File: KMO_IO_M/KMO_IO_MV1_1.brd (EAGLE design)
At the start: 84.5 x 96.5 mm, 68 parts, among them Q1 8MHz, Q2 25MHz, U1 ATMEGA328

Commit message: IO BL rev
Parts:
- added D1, D2: M7, SparkFun-DiscreteSemi:SMA-DIODE
- added IC1, IC2, IC3, IC4, IC5, IC6, IC7: 100p, SparkFun-Passives:0805
- added ID1, ID2, ID3, ID4, ID5, ID6, ID7: 3V3, diode:SOT23
- added IIR1, IIR2, IIR3, IIR4, IIR5, IIR6, IIR7: 22, SparkFun-Passives:0805
- added OL1, OL2, OL3: YLW, led:CHIP-LED0805
- added OLR1, OLR2, OLR3: 330, SparkFun-Passives:0805
- INDL: value BLUE -> BLU
- PL: value RED -> GRN
- moved U$1 46.3 mm to (16.0, 52.5)
- moved C2 6.39 mm to (55.0, 80.5), turned to 180 degrees
- moved R2 3.82 mm to (51.5, 84.0), turned to 90 degrees
- moved IR7 3.18 mm to (11.2, 5.00), turned to 90 degrees
- moved U$4 2.85 mm to (20.0, 8.00)
- moved IR4 2.24 mm to (11.5, 21.8), turned to 90 degrees
- moved IR1 2.14 mm to (11.5, 37.0), turned to 90 degrees
- moved IR2 2.14 mm to (11.5, 32.0), turned to 90 degrees
- moved IR3 2.14 mm to (11.5, 27.0), turned to 90 degrees
- moved IR5 2.14 mm to (11.5, 16.8), turned to 90 degrees
- moved IR6 2.14 mm to (11.5, 11.5), turned to 90 degrees
- moved C3 1.82 mm to (48.2, 79.5)
- moved C1 1.35 mm to (48.2, 75.2)
- moved OD3 0.56 mm to (17.5, 63.8)
- moved XO 0.25 mm to (2.00, 77.8)
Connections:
- new net A10: IC4.1, ID4.3, IIR4.1
- new net A11: IC5.1, ID5.3, IIR5.1
- new net A12: IC6.1, ID6.3, IIR6.1
- new net A13: IC7.1, ID7.3, IIR7.1
- new net A8: IC2.1, ID2.3, IIR2.1
- new net A9: IC3.1, ID3.3, IIR3.1
- new net BLG: BL.6, C1.1, D2.A, INDL.C, Q1.2, SR.2, U1.21, U1.3, U1.5
- new net BLV: BL.2, C3.2, D1.C, R1.2, R2.2, R3.2, U1.18, U1.4, U1.6
- new net N$12: IIR1.2, XI.4
- new net N$20: IIR2.2, XI.5
- new net N$21: IIR3.2, XI.6
- new net N$23: IIR4.2, XI.7
- new net N$25: IIR5.2, XI.8
- new net N$26: IIR6.2, XI.9
- new net N$27: IIR7.2, XI.10
- new net N$6: OL3.A, OLR3.1
- new net N$7: OL1.A, OLR1.1
- new net N$8: OL2.A, OLR2.1
- net +3V3: now also D1.A; no longer BL.2, C3.2, R1.2, R2.2, R3.2, U1.18, U1.4, U1.6
- net A1: now also IC1.1, ID1.3, IIR1.1; no longer XI.4
- net A2: no longer XI.5
- net A3: no longer XI.6
- net A4: no longer XI.7
- net A5: no longer XI.8
- net A6: no longer XI.9
- net A7: no longer XI.10
- net D5: now also OLR3.2
- net D6: now also OLR2.2
- net D7: now also OLR1.2
- net GND: now also D2.C, IC1.2, IC2.2, IC3.2, IC4.2, IC5.2, IC6.2, IC7.2, ID1.1, ID2.1, ID3.1, ID4.1, ID5.1, ID6.1, ID7.1, OL1.C, OL2.C, OL3.C; no longer BL.6, C1.1, INDL.C, Q1.2, SR.2, U1.21, U1.3, U1.5
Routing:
- net BLG: track 0.00 -> 143.3 mm, vias 0 -> 1
- net BLV: track 0.00 -> 88.4 mm, vias 0 -> 2
- net +3V3: track 338.9 -> 274.4 mm, vias 9 -> 3
- net D6: track 31.5 -> 66.2 mm, vias 0 -> 3
- net D5: track 33.4 -> 60.6 mm
- net A4: track 98.1 -> 72.6 mm, vias 2 -> 3
- net A6: track 122.6 -> 101.2 mm, vias 1 -> 2
- net GND: track 489.6 -> 509.0 mm, vias 2 -> 7
- net A1: track 79.8 -> 61.0 mm, vias 1 -> 2
- net D12: track 89.3 -> 71.5 mm, vias 2 -> 3
- net DTR: track 68.0 -> 50.5 mm
- net A0: track 49.6 -> 33.1 mm, vias 1 -> 0
- net RAW_IV: track 187.8 -> 172.6 mm, vias 0 -> 2
- net A5: track 90.3 -> 104.8 mm, vias 1 -> 0
- net TD+: track 35.2 -> 49.5 mm, vias 2 -> 0
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
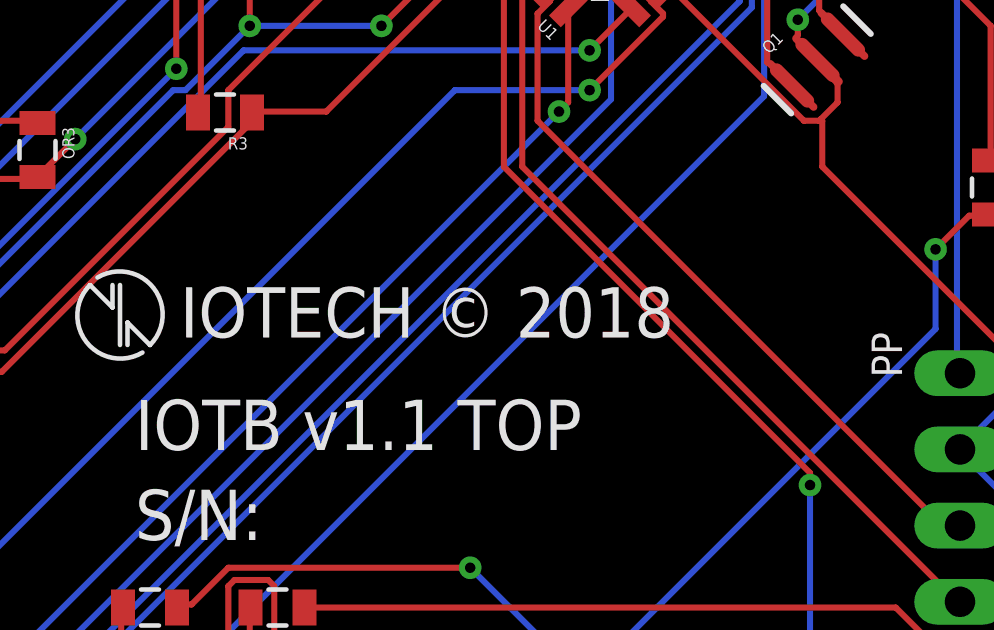
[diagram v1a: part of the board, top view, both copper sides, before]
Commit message: 1.1 inductance value rev
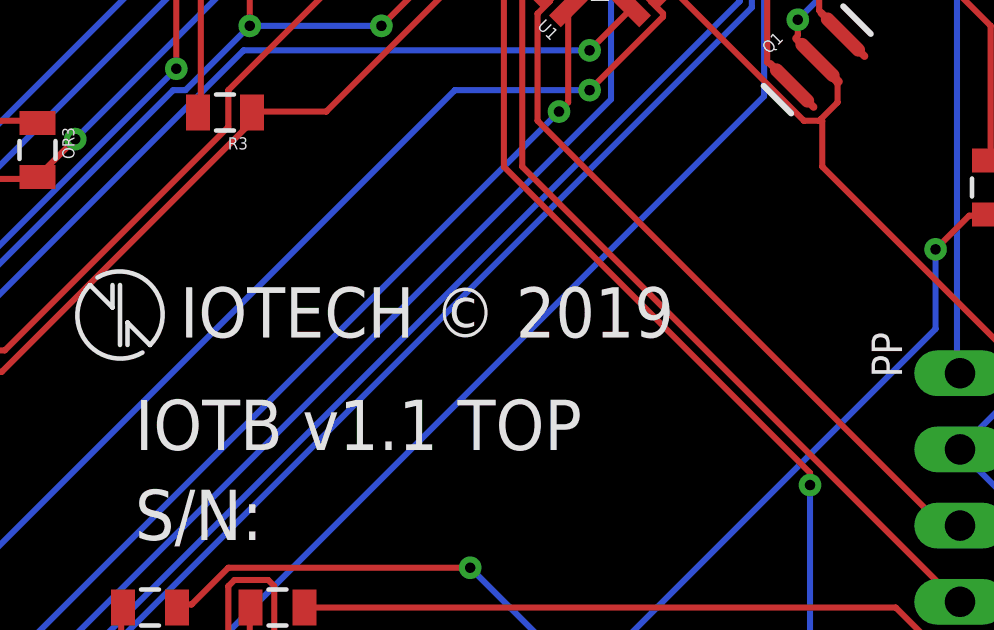
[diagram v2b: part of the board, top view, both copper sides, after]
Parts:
- PC1: value 680uf -> 470uf
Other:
- board text added: "IOTECH © 2019"
- board text removed: "IOTECH © 2018"
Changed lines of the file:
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@@
 <wire x1="84.5" y1="0" x2="0" y2="0" width="0.1524" layer="20" locked="yes"/>
 <text x="44.75" y="52.5" size="1.6764" layer="21">IOTB v1.1 TOP</text>
-<text x="46.25" y="56.25" size="1.6764" layer="21">IOTECH © 2018</text>
+<text x="46.25" y="56.25" size="1.6764" layer="21">IOTECH © 2019</text>
 <wire x1="44" y1="57.25" x2="43.25" y2="58" width="0.1524" layer="21"/>
 <wire x1="44.5" y1="56.75" x2="45.25" y2="56" width="0.1524" layer="21"/>
@@
 <attribute name="VALUE" x="48.766" y="65.147" size="0.4064" layer="27" rot="R180"/>
 </element>
-<element name="PC1" library="rcl" library_urn="urn:adsk.eagle:library:334" package="140CLH-1010" package3d_urn="urn:adsk.eagle:package:23391/1" value="680uf" x="32.75" y="23.5" smashed="yes" rot="R270">
+<element name="PC1" library="rcl" library_urn="urn:adsk.eagle:library:334" package="140CLH-1010" package3d_urn="urn:adsk.eagle:package:23391/1" value="470uf" x="32.75" y="23.5" smashed="yes" rot="R270">
 <attribute name="NAME" x="34.68" y="26.24" size="1.27" layer="25" rot="R270"/>
 <attribute name="SPICEPREFIX" value="C" x="32.75" y="23.5" size="1.778" layer="27" rot="R270" display="off"/>

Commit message: out led rev
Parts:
- removed OLR1, OLR2, OLR3: 330, SparkFun-Passives:0805
- PR1: value 470 -> 1k
- R6: value 330 -> 1k
- turned EC3 to 270 degrees
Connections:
- net BLG: now also C3.2
- net BLV: now also C3.1; no longer C3.2
- net D5: no longer OLR3.2
- net D6: no longer OLR2.2
- net D7: no longer OLR1.2
- net GND: no longer C3.1, OR1.1, OR2.1, OR3.1
- net N$6: now also OR3.1; no longer OLR3.1
- net N$7: now also OL2.A, OR2.1; no longer OL1.A, OLR1.1
- net N$8: now also OL1.A, OR1.1; no longer OL2.A, OLR2.1
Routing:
- net GND: track 509.0 -> 551.8 mm, vias 7 -> 5
- net D6: track 66.2 -> 31.5 mm, vias 3 -> 0
- net D7: track 66.4 -> 35.5 mm
- net N$8: track 4.76 -> 35.0 mm
- net A5: track 104.8 -> 75.7 mm, vias 0 -> 3
- net N$7: track 4.26 -> 32.7 mm
- net D5: track 60.6 -> 33.4 mm
- net N$6: track 6.44 -> 33.2 mm
- net D13: track 116.0 -> 141.0 mm
- net DTR: track 50.5 -> 72.5 mm, vias 1 -> 0
- net A6: track 101.2 -> 122.7 mm, vias 2 -> 0
- net A2: track 83.2 -> 63.2 mm, vias 2 -> 0
- net A7: track 91.7 -> 111.4 mm
- net A3: track 86.2 -> 69.0 mm, vias 2 -> 0
- net D11: track 72.1 -> 88.7 mm, vias 3 -> 2
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
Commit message: al con
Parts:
- PC1: value 470uf -> 470uf 25v
- PC2: value 220uf -> 220uf 50v
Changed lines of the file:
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@@
 <attribute name="VALUE" x="48.766" y="65.147" size="0.4064" layer="27" rot="R180"/>
 </element>
-<element name="PC1" library="rcl" library_urn="urn:adsk.eagle:library:334" package="140CLH-1010" package3d_urn="urn:adsk.eagle:package:23391/1" value="470uf" x="32.75" y="23.5" smashed="yes" rot="R270">
+<element name="PC1" library="rcl" library_urn="urn:adsk.eagle:library:334" package="140CLH-1010" package3d_urn="urn:adsk.eagle:package:23391/1" value="470uf 25v" x="32.75" y="23.5" smashed="yes" rot="R270">
 <attribute name="NAME" x="34.68" y="26.24" size="1.27" layer="25" rot="R270"/>
 <attribute name="SPICEPREFIX" value="C" x="32.75" y="23.5" size="1.778" layer="27" rot="R270" display="off"/>
 <attribute name="VALUE" x="29.865" y="26.875" size="1.27" layer="27" rot="R270"/>
 </element>
-<element name="PC2" library="rcl" library_urn="urn:adsk.eagle:library:334" package="140CLH-1010" package3d_urn="urn:adsk.eagle:package:23391/1" value="220uf" x="59.75" y="15.5" smashed="yes" rot="R270">
+<element name="PC2" library="rcl" library_urn="urn:adsk.eagle:library:334" package="140CLH-1010" package3d_urn="urn:adsk.eagle:package:23391/1" value="220uf 50v" x="59.75" y="15.5" smashed="yes" rot="R270">
 <attribute name="NAME" x="61.68" y="18.24" size="1.27" layer="25" rot="R270"/>
 <attribute name="SPICEPREFIX" value="C" x="59.75" y="15.5" size="1.778" layer="27" rot="R270" display="off"/>

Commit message: 11 ok
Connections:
- net D11: now also BL.4, U1.15; no longer BL.1, U1.16
- net D12: now also BL.1, U1.16; no longer BL.4, U1.15
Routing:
- net GND: track 551.8 -> 575.6 mm, vias 5 -> 4
- net A7: track 111.4 -> 128.0 mm
- net RAW_IV: track 163.5 -> 179.9 mm, vias 2 -> 1
- net BLG: track 130.1 -> 142.7 mm
- net D11: track 88.7 -> 77.7 mm, vias 2 -> 4
- net D12: track 77.1 -> 86.5 mm
- net TXO: track 28.7 -> 23.9 mm
- net RESET: track 103.8 -> 108.2 mm, vias 2 -> 1
- net A0: track 31.1 -> 35.2 mm
- net D3: track 49.3 -> 53.2 mm, vias 2 -> 1
- net RXI: track 30.8 -> 27.2 mm
- net D4: track 55.3 -> 57.5 mm
- net A1: track 64.0 -> 66.1 mm
- net D10: track 61.3 -> 62.6 mm, vias 2 -> 4
- net +3V3: track 279.6 -> 278.4 mm
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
